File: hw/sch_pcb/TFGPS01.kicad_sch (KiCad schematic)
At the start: 74 parts, among them J1 SM10B-GHS-TB, J2 USBC_USB4105-GF-A, J3 SM06B-GHS-TB, J4 SM04B-GHS-TB, J5 SM08B-GHS-TB, M1 HOLE, M2 HOLE, M3 HOLE, M4 HOLE, Q1 BC817-25, Q2 BC817-25, Q3 BC817-25, U1 MIC5504-3.3YM5, U2 USBLC6-2SC6, U3 NEO-M8P, U4 MAX2655

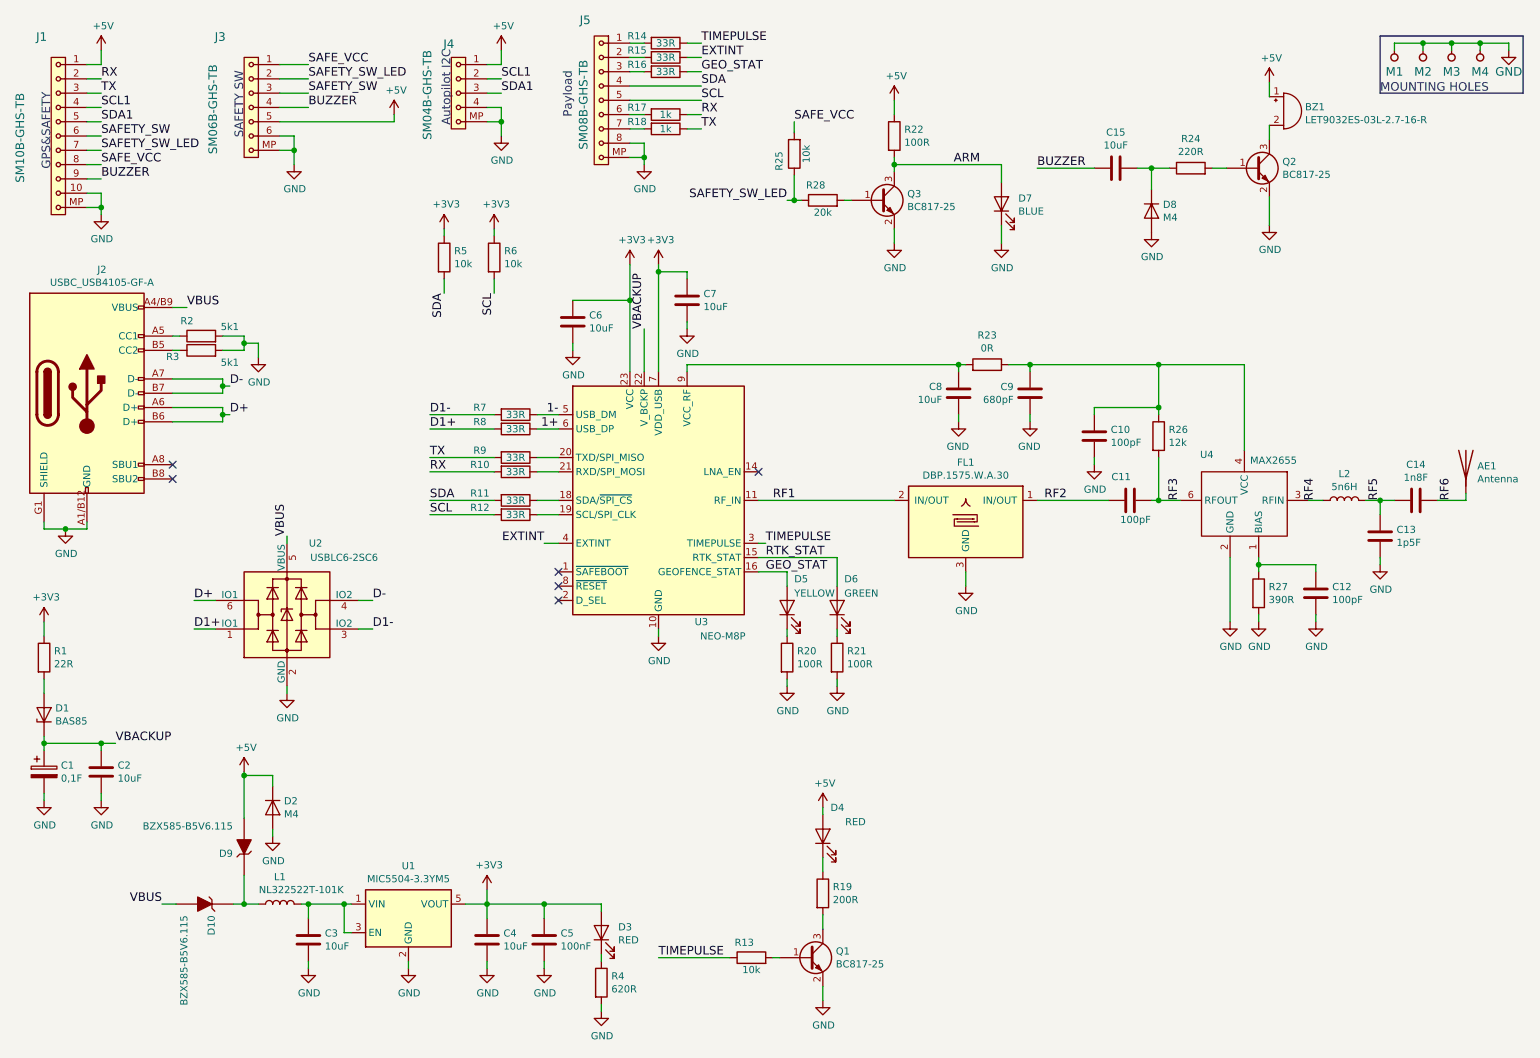
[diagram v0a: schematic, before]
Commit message: Update project to KiCADv9.
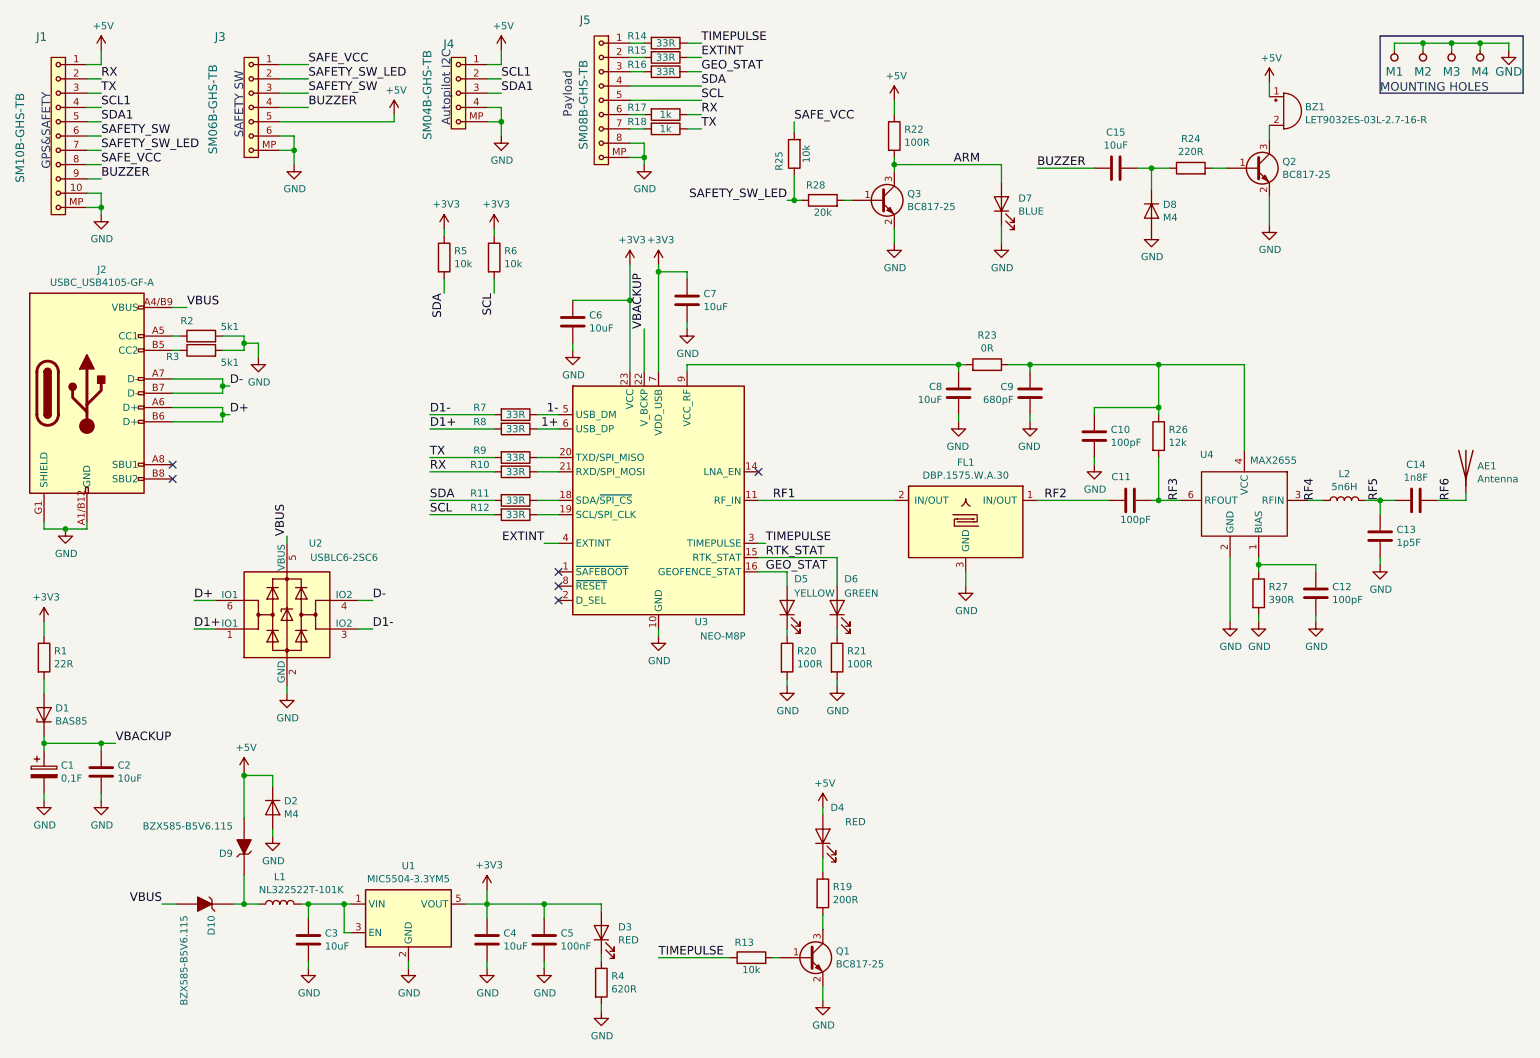
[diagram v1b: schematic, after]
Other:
- title: TFGPS01A -> TFGPS01C

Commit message: Resolved #35
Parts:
- added G1: LOGO, TF_LOGA:TF 14x6,6, symbol TF_LOGO:LOGO
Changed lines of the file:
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@@
+	)
+	(symbol
+		(lib_id "TF_LOGO:LOGO")
+		(at 257.81 67.31 0)
+		(unit 1)
+		(exclude_from_sim no)
+		(in_bom no)
+		(on_board yes)
+		(dnp no)
+		(fields_autoplaced yes)
+		(property "Reference" "G1"
+			(at 272.0731 67.31 0)
+			(effects
+				(font
+					(size 1.27 1.27)
+				)
+				(justify left)
+			)
+		)
+		(property "Value" "LOGO"
+			(at 257.81 73.7776 0)
+			(effects
+				(font
+					(size 1.27 1.27)
+				)
+				(hide yes)
+			)
+		)
+		(property "Footprint" "TF_LOGA:TF 14x6,6"
+			(at 257.81 67.31 0)
+			(effects
+				(font
+					(size 1.27 1.27)
+				)
+				(hide yes)
+			)
+		)
+		(property "Datasheet" ""
+			(at 257.81 67.31 0)
+			(effects
+				(font
+					(size 1.27 1.27)
+				)
+				(hide yes)
+			)
+		)
+		(property "Description" ""
+			(at 257.81 67.31 0)
+			(effects
+				(font
+					(size 1.27 1.27)
+				)
+				(hide yes)
+			)
+		)
+		(property "UST_ID" ""
+			(at 257.81 67.31 0)
+			(effects
+				(font
+					(size 1.27 1.27)
+				)
+				(hide yes)
+			)
+		)
+		(instances
+			(project ""
+				(path "/73a4ed73-0a5d-4a8d-ac5b-dfe222bafbe2"
+					(reference "G1")
+					(unit 1)
+				)
+			)
+		)
 	)
 	(symbol

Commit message: Resolve  #34.
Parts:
- R24: value 220R -> 1k; UST_ID 5c70984512875079b91f897f -> 5c70984512875079b91f898c
- R4: value 620R -> 200R; UST_ID 5c70984512875079b91f8989 -> 5c70984512875079b91f897d
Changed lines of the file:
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@@
 			)
 		)
-		(property "Value" "620R"
+		(property "Value" "200R"
 			(at 119.888 185.928 0)
 			(effects
@@
 			)
 		)
-		(property "UST_ID" "5c70984512875079b91f8989"
+		(property "UST_ID" "5c70984512875079b91f897d"
 			(at 118.11 184.785 0)
 			(effects
@@
 			)
 		)
-		(property "Value" "220R"
+		(property "Value" "1k"
 			(at 222.885 37.078 90)
 			(effects
@@
 			)
 		)
-		(property "UST_ID" "5c70984512875079b91f897f"
+		(property "UST_ID" "5c70984512875079b91f898c"
 			(at 222.885 40.005 0)
 			(effects

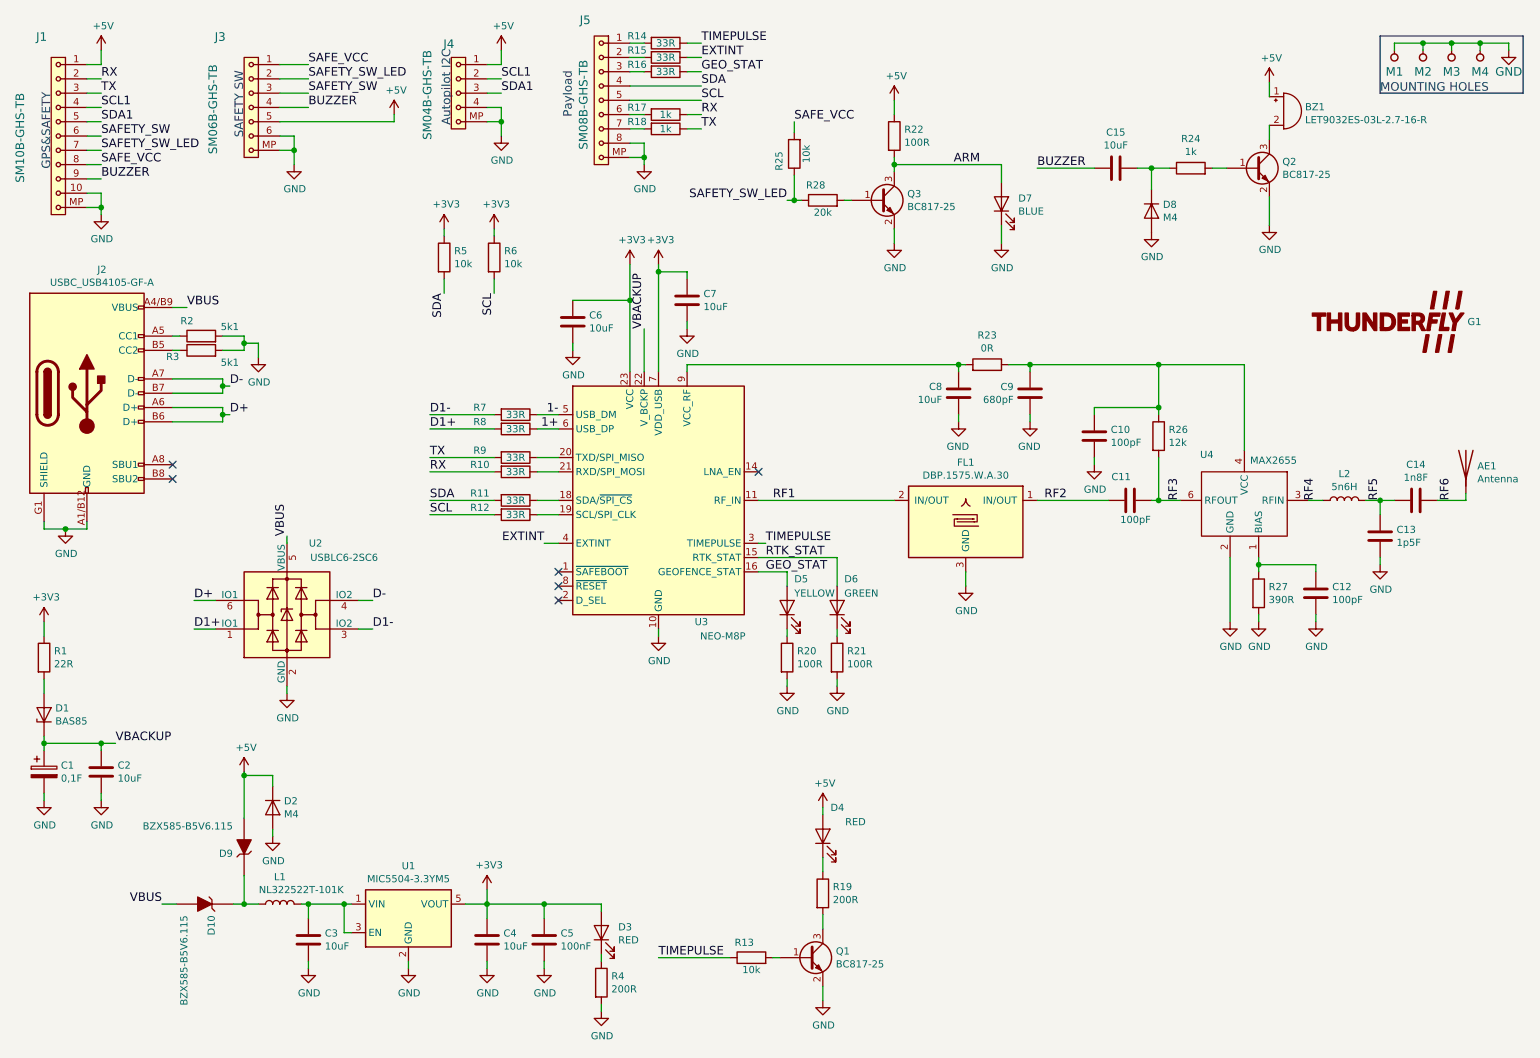
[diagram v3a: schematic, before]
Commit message: Fix #32. Added 5VA symbol for Autopilot 5V power.
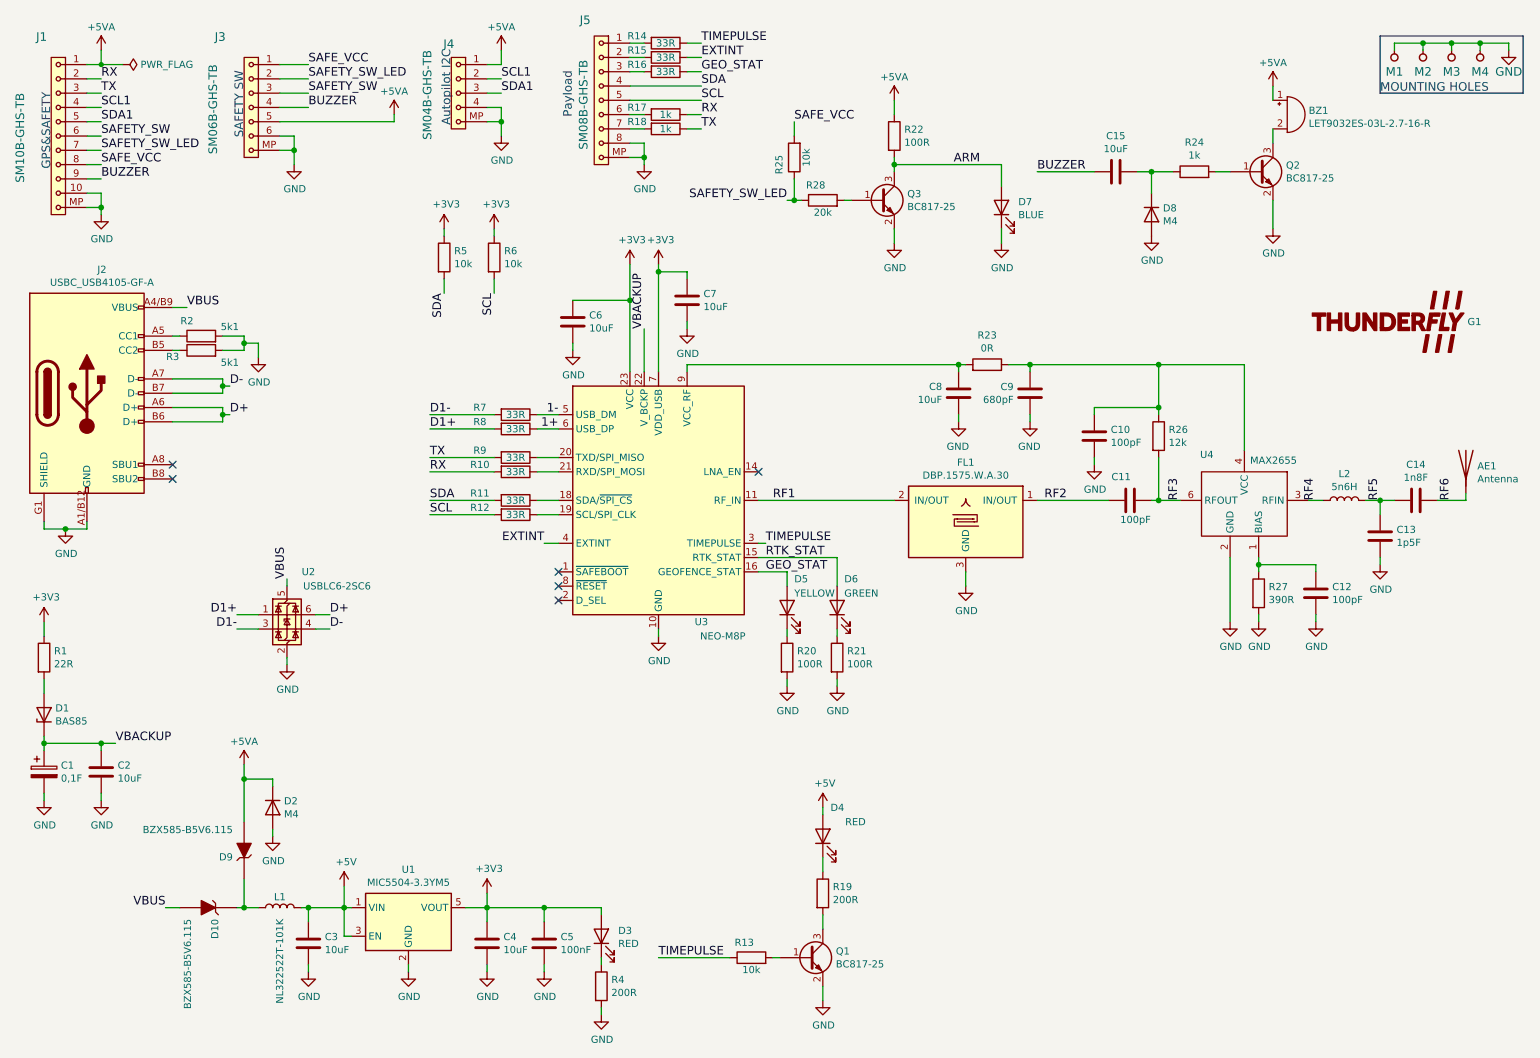
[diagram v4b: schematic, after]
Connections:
- net +5V: now also C3.1, L1.2, U1.1 (VIN), U1.3 (EN); no longer BZ1.1 (-), D2.1 (K), D9.2 (A), J1.1, J3.5, J4.1, R22.1
- new net +5VA: BZ1.1 (+), D2.1 (K), D9.2 (A), J1.1, J3.5, J4.1, R22.1
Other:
- moved on the sheet: BZ1, C15, C3, C4, C5, D10, D3, D7, D8, D9, L1, Q2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
